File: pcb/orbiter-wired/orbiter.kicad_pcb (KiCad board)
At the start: 2 copper layers, 140 x 91 mm, 144 parts, among them J1 SWD, J2 AudioJack4, J3 SWD, J4 AudioJack4, SW1 SW_SPDT, SW10 SW_Push, SW11 SW_Push, SW12 SW_Push, SW13 SW_Push, SW14 SW_Push, SW15 SW_Push, SW16 SW_Push, SW17 SW_Push, SW18 SW_Push, SW19 SW_Push, SW2 SW_Push, SW20 SW_Push, SW21 SW_Push, SW22 SW_Push, SW23 SW_Push, SW24 SW_Push, SW25 SW_Push, SW26 SW_Push, SW27 SW_Push, SW28 SW_SPDT, SW3 SW_Push, SW4 SW_Push, SW5 SW_Push, SW6 SW_Push, SW7 SW_Push, SW8 SW_Push, SW9 SW_Push, U1 TPS82140

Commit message: Add crude version text
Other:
- board text added: "v1.0"
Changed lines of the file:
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@@
 		(layer "Edge.Cuts")
+	)
+	(gr_text "v1.0"
+		(at 75.825 114.025 -0)
+		(layer "B.SilkS")
+		(effects
+			(font
+				(size 1 1)
+				(thickness 0.25)
+				(bold yes)
+			)
+			(justify left bottom mirror)
+		)
 	)
 	(gr_text "RIGHT"
@@
 				(bold yes)
 			)
+			(justify left bottom)
+		)
+	)
+	(gr_text "v1.0"
+		(at 83.275 114.1 0)
+		(layer "F.SilkS")
+		(effects
+			(font
+				(size 1 1)
+				(thickness 0.25)
+				(bold yes)
+			)

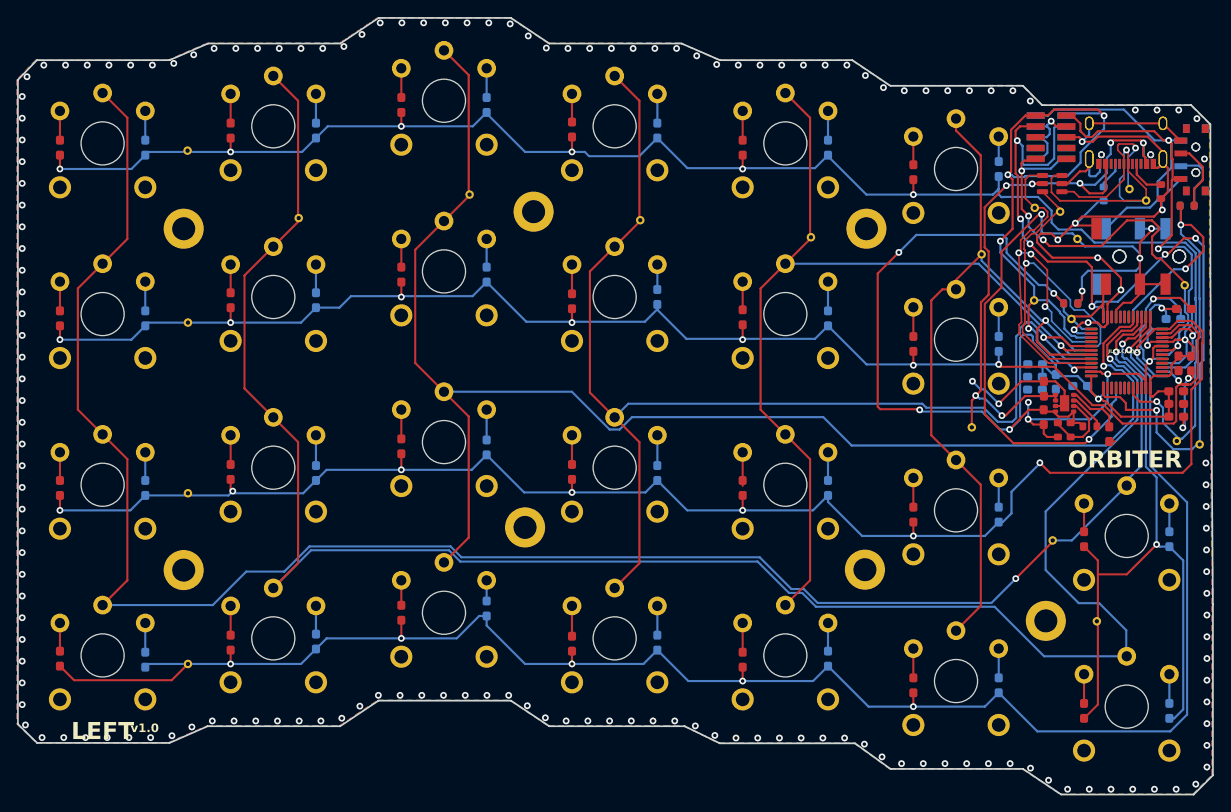
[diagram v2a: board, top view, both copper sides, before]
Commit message: Move diodes away from kb switch
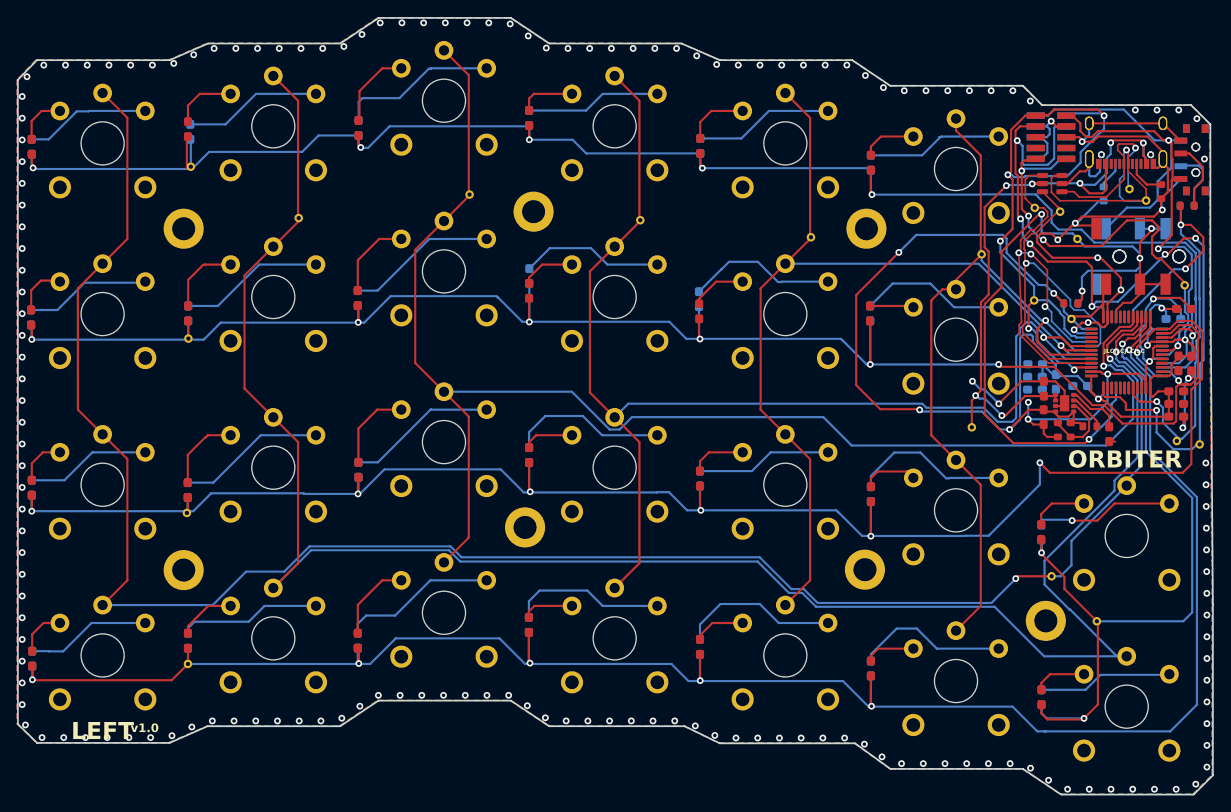
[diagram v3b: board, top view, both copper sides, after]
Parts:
- moved D28 15.6 mm to (109.9, 103.3)
- moved D50 15.5 mm to (169.9, 64.9)
- moved D26 15.3 mm to (109.9, 63.1)
- moved D42 15.3 mm to (149.9, 63.2)
- moved D27 15.3 mm to (110.0, 83.2)
- moved D25 15.2 mm to (110.0, 43.2)
- moved D34 15.2 mm to (130.0, 60.5)
- moved D36 15.2 mm to (129.9, 101.4)
- moved D35 15.2 mm to (130.0, 81.5)
- moved D51 15.2 mm to (170.0, 86.1)
- moved D18 15.2 mm to (90.0, 85.6)
- moved D52 15.1 mm to (170.0, 106.5)
- moved D33 15.1 mm to (130.0, 42.0)
- moved D44 15.1 mm to (150.0, 104.0)
- moved D20 15.1 mm to (190.0, 109.9)
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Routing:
- net /T_KEY_ROW1: track 176.8 -> 198.4 mm, vias 8 -> 7
- net /T_KEY_ROW2: track 189.1 -> 209.9 mm, vias 8 -> 7
- net Net-(D28-A): track 2.42 -> 18.3 mm
- net Net-(D25-A): track 3.42 -> 18.8 mm
- net Net-(D44-A): track 3.30 -> 18.7 mm
- net Net-(D51-A): track 3.42 -> 18.6 mm
- net Net-(D35-A): track 3.55 -> 18.5 mm
- net Net-(D36-A): track 3.42 -> 18.2 mm
- net Net-(D52-A): track 3.42 -> 18.0 mm
- net Net-(D26-A): track 3.30 -> 17.6 mm
- net Net-(D42-A): track 3.42 -> 17.6 mm
- net Net-(D27-A): track 3.55 -> 17.6 mm
- net /T_KEY_ROW3: track 211.3 -> 225.2 mm
- net Net-(D34-A): track 2.92 -> 16.8 mm
- net Net-(D50-A): track 3.42 -> 17.3 mm
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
